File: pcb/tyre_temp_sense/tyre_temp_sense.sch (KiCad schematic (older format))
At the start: 40 parts, among them J1 Conn_01x04_Male, J2 POWER & CAN, J3 Conn_01x08_Male, J4 Conn_01x04, J5 Conn_01x04, J6 Conn_01x04, J7 Conn_01x04, J8 Conn_01x02, U1 TCA9548APWR, U2 MCP2515-xST, U3 MCP2551-I-SN, Y1 8 mhz

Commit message: Updates
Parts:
- C1, C2, C3, C4: footprint (none) -> Capacitor_SMD:C_0603_1608Metric
- J2: renamed from J3; value Conn_01x08_Male -> Extra i2c ports (no pullups); footprint (none) -> Connector_PinHeader_2.54mm:PinHeader_1x08_P2.54mm_Vertical
- J3: renamed from J1; value Conn_01x04_Male -> Analog breakout; footprint (none) -> Connector_PinHeader_2.54mm:PinHeader_1x04_P2.54mm_Vertical
- J4: value Conn_01x04 -> MUX Port 0; footprint (none) -> Connector_JST:JST_EH_B4B-EH-A_1x04_P2.50mm_Vertical
- J5: value Conn_01x04 -> MUX Port 1; footprint (none) -> Connector_JST:JST_EH_B4B-EH-A_1x04_P2.50mm_Vertical
- J6: value Conn_01x04 -> MUX Port 2; footprint (none) -> Connector_JST:JST_EH_B4B-EH-A_1x04_P2.50mm_Vertical
- J7: value Conn_01x04 -> MUX Port 3; footprint (none) -> Connector_JST:JST_EH_B4B-EH-A_1x04_P2.50mm_Vertical
- R1, R10, R11, R12, R13, R14, R2, R3, R4, R5, R6, R7, R8, R9: footprint (none) -> Resistor_SMD:R_0603_1608Metric
- TP1: renamed from TP6; value TestPoint -> CAN_H
- TP2: renamed from TP7; value TestPoint -> GND
- TP3: renamed from TP8; value TestPoint -> CAN_L
- TP4: renamed from TP9; value TestPoint -> 5V
- TP5: renamed from TP1; value TestPoint -> MOSI
- TP6: renamed from TP2; value TestPoint -> MISO
- TP7: renamed from TP3; value TestPoint -> CLK
- TP8: renamed from TP4; value TestPoint -> RX
- TP9: renamed from TP5; value TestPoint -> TX
- U2: value MCP2515-xST -> MCP2515-I/ST; LCSC (none) -> C15193
- Y1: JLCPCB Part # (none) -> C403948
- renumbered J2 to J1
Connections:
- net at U1.13 (SD4): now also J2.1 (Pin_1); no longer J2.7 (Pin_7)
- net at U1.14 (SC4): now also J2.2 (Pin_2); no longer J2.8 (Pin_8)
- net at U1.15 (SD5): now also J2.3 (Pin_3); no longer J2.5 (Pin_5)
- net at U1.16 (SC5): now also J2.4 (Pin_4); no longer J2.6 (Pin_6)
- net at U1.17 (SD6): now also J2.5 (Pin_5); no longer J2.3 (Pin_3)
- net at U1.18 (SC6): now also J2.6 (Pin_6); no longer J2.4 (Pin_4)
- net at U1.19 (SD7): now also J2.7 (Pin_7); no longer J2.1 (Pin_1)
- net at U1.20 (SC7): now also J2.8 (Pin_8); no longer J2.2 (Pin_2)
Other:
- note added: "4 pin JST connector for each temp sensor"
- note added: "AUMT tyre temperature sensing control board"
- note added: "Arduino Nano"
- note added: "CAN Controller\n"
- note added: "CAN Transceiver\n"
- note added: "Input power and CAN\n"
- moved on the sheet: A1, C1, C2, C3, C4, J1, J2, J3, J4, J5, J6, J7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

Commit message: Second revision
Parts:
- removed J2: Extra i2c ports (no pullups), Connector_PinHeader_2.54mm:PinHeader_1x08_P2.54mm_Vertical, symbol Connector:Conn_01x08_Male
- removed TP2: GND, TestPoint:TestPoint_Pad_D1.5mm, symbol Connector:TestPoint
- removed TP4: 5V, TestPoint:TestPoint_Pad_D1.5mm, symbol Connector:TestPoint
- removed TP5: MOSI, TestPoint:TestPoint_Pad_D1.5mm, symbol Connector:TestPoint
- removed TP6: MISO, TestPoint:TestPoint_Pad_D1.5mm, symbol Connector:TestPoint
- removed TP7: CLK, TestPoint:TestPoint_Pad_D1.5mm, symbol Connector:TestPoint
- added J8, J9: GND, Connector_PinHeader_2.54mm:PinHeader_1x04_P2.54mm_Vertical, symbol tyre_temp_sense-rescue:Conn_01x04_Male-Connector
- A1: symbol MCU_Module:Arduino_Nano_v3.x -> tyre_temp_sense-rescue:Arduino_Nano_v3.x-MCU_Module
- C1: renamed from C2; symbol Device:C -> tyre_temp_sense-rescue:C-Device
- C2: renamed from C3; symbol Device:C -> tyre_temp_sense-rescue:C-Device
- C3: renamed from C1; symbol Device:C -> tyre_temp_sense-rescue:C-Device
- C4: symbol Device:C -> tyre_temp_sense-rescue:C-Device
- J1: symbol Connector_Generic:Conn_01x04 -> tyre_temp_sense-rescue:Conn_01x04-Connector_Generic
- J2: renamed from J4; symbol Connector_Generic:Conn_01x04 -> tyre_temp_sense-rescue:Conn_01x04-Connector_Generic
- J3: renamed from J5; symbol Connector_Generic:Conn_01x04 -> tyre_temp_sense-rescue:Conn_01x04-Connector_Generic
- J4: renamed from J6; symbol Connector_Generic:Conn_01x04 -> tyre_temp_sense-rescue:Conn_01x04-Connector_Generic
- J5: renamed from J7; symbol Connector_Generic:Conn_01x04 -> tyre_temp_sense-rescue:Conn_01x04-Connector_Generic
- J6: renamed from J8; symbol Connector_Generic:Conn_01x02 -> tyre_temp_sense-rescue:Conn_01x02-Connector_Generic
- J7: renamed from J3; value Analog breakout -> A; symbol Connector:Conn_01x04_Male -> tyre_temp_sense-rescue:Conn_01x04_Male-Connector; Note Breakout extra analogue pins from arduino -> (none)
- R1, R10, R11, R12, R13, R2, R3, R4, R5, R6, R7, R8, R9: symbol Device:R -> tyre_temp_sense-rescue:R-Device
- R14: footprint Resistor_SMD:R_0603_1608Metric -> Resistor_SMD:R_1210_3225Metric; symbol Device:R -> tyre_temp_sense-rescue:R-Device
- TP1, TP3, TP8, TP9: symbol Connector:TestPoint -> tyre_temp_sense-rescue:TestPoint-Connector
- U1: symbol Interface_Expansion:TCA9548APWR -> tyre_temp_sense-rescue:TCA9548APWR-Interface_Expansion
- U2: symbol Interface_CAN_LIN:MCP2515-xST -> tyre_temp_sense-rescue:MCP2515-xST-Interface_CAN_LIN; LCSC C15193 -> (none)
- U3: symbol Interface_CAN_LIN:MCP2551-I-SN -> tyre_temp_sense-rescue:MCP2551-I-SN-Interface_CAN_LIN
- Y1: footprint (none) -> Crystal:Crystal_SMD_5032-2Pin_5.0x3.2mm; symbol Device:Crystal -> tyre_temp_sense-rescue:Crystal-Device; JLCPCB Part # C403948 -> C115962
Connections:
- net +3V3: now also J2.4 (Pin_4), J3.4 (Pin_4), J4.4 (Pin_4), J5.4 (Pin_4); no longer J2.2 (Pin_2), J3.2 (Pin_2), J4.2 (Pin_2), J5.2 (Pin_2)
- net +5V: now also J9.1 (Pin_1), J9.2 (Pin_2), J9.3 (Pin_3), J9.4 (Pin_4)
- net GND: now also J2.3 (Pin_3), J3.3 (Pin_3), J4.3 (Pin_3), J5.3 (Pin_3), J8.1 (Pin_1), J8.2 (Pin_2), J8.3 (Pin_3), J8.4 (Pin_4); no longer J2.1 (Pin_1), J3.1 (Pin_1), J4.1 (Pin_1), J5.1 (Pin_1)
- net A0: now reaches A1.19 (A0), J7.4 (Pin_4)
- net A1: now reaches A1.20 (A1), J7.3 (Pin_3)
- net A2: now reaches A1.21 (A2), J7.2 (Pin_2)
- net A3: now reaches A1.22 (A3), J7.1 (Pin_1)
- net at R11.2, U1.10 (SD3): now also J5.1 (Pin_1); no longer J5.4 (Pin_4)
- net at R10.2, U1.11 (SC3): now also J5.2 (Pin_2); no longer J5.3 (Pin_3)
- net at R5.2, U1.4 (SD0): now also J2.1 (Pin_1); no longer J2.4 (Pin_4)
- net at R4.2, U1.5 (SC0): now also J2.2 (Pin_2); no longer J2.3 (Pin_3)
- net at R7.2, U1.6 (SD1): now also J3.1 (Pin_1); no longer J3.4 (Pin_4)
- net at R6.2, U1.7 (SC1): now also J3.2 (Pin_2); no longer J3.3 (Pin_3)
- net at R9.2, U1.8 (SD2): now also J4.1 (Pin_1); no longer J4.4 (Pin_4)
- net at R8.2, U1.9 (SC2): now also J4.2 (Pin_2); no longer J4.3 (Pin_3)
- net CAN_H renamed CAN+
- net CAN+: now also J1.3 (Pin_3), TP3.1; no longer J1.4 (Pin_4), TP1.1
- net CAN_L renamed CAN-
- net CAN-: now also J1.4 (Pin_4), TP1.1; no longer J1.3 (Pin_3), TP3.1
- no-connect marks 20 -> 28
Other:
- note removed: "Breakout extra i2c connections\n"
- moved on the sheet: C3, J2, J3, J4, J5, J7, R1, R10, R11, R2, R3, R4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

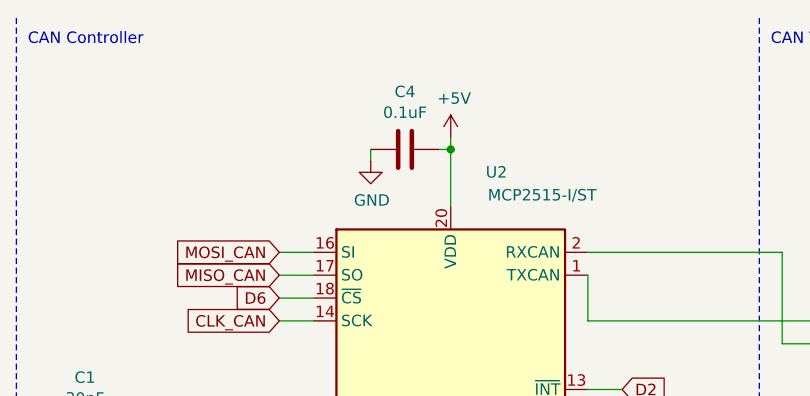
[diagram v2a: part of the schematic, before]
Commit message: Added LCSC Part info
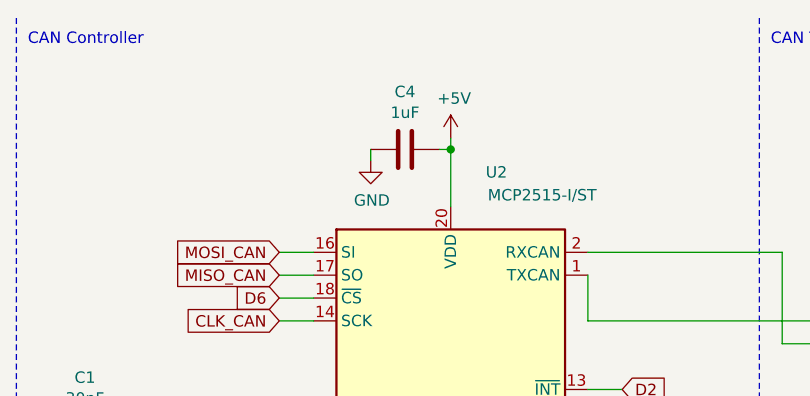
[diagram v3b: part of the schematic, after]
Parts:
- C1, C2: LCSC (none) -> C22397
- C3: LCSC (none) -> C19702
- C4: value 0.1uF -> 1uF; LCSC (none) -> C15849
- R1, R12, R13: LCSC (none) -> C25804
- R10, R11, R2, R3, R4, R5, R6, R7, R8, R9: LCSC (none) -> C23162
- R14: footprint Resistor_SMD:R_1210_3225Metric -> Resistor_SMD:R_1206_3216Metric; LCSC (none) -> C22107
- U1: LCSC (none) -> C130026
- U2: LCSC (none) -> C15193
- U3: LCSC (none) -> C49558
- Y1: JLCPCB Part # C115962 -> (none); LCSC (none) -> C115962
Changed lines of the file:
@@
 F 2 "Package_SO:TSSOP-20_4.4x6.5mm_P0.65mm" H 6650 1200 50  0001 C CIN
 F 3 "https://datasheet.lcsc.com/lcsc/1809191814_Microchip-Tech-MCP2515-I-ST_C15193.pdf" H 6750 1300 50  0001 C CNN
+F 4 "C15193" H 6650 2100 50  0001 C CNN "LCSC"
 	1    6650 2100
 	1    0    0    -1
@@
 F 1 "MCP2551-I-SN" H 8900 2500 50  0000 C CNN
 F 2 "Package_SO:SOIC-8_3.9x4.9mm_P1.27mm" H 9350 1500 50  0001 C CIN
-F 3 "http://ww1.microchip.com/downloads/en/devicedoc/21667d.pdf" H 9350 2000 50  0001 C CNN
+F 3 "https://datasheet.lcsc.com/lcsc/1809192221_Microchip-Tech-MCP2551T-I-SN_C49558.pdf" H 9350 2000 50  0001 C CNN
+F 4 "C49558" H 9350 2000 50  0001 C CNN "LCSC"
 	1    9350 2000
 	1    0    0    -1
@@
 P 6450 1050
 F 0 "C4" V 6198 1050 50  0000 C CNN
-F 1 "0.1uF" V 6289 1050 50  0000 C CNN
+F 1 "1uF" V 6289 1050 50  0000 C CNN
 F 2 "Capacitor_SMD:C_0603_1608Metric" H 6488 900 50  0001 C CNN
-F 3 "~" H 6450 1050 50  0001 C CNN
+F 3 "https://datasheet.lcsc.com/lcsc/1810261812_Samsung-Electro-Mechanics-CL10A105KB8NNNC_C15849.pdf" H 6450 1050 50  0001 C CNN
+F 4 "C15849" V 6450 1050 50  0001 C CNN "LCSC"
 	1    6450 1050
 	0    1    1    0
@@
 F 1 "30pF" V 4889 2300 50  0000 C CNN
 F 2 "Capacitor_SMD:C_0603_1608Metric" H 5088 2150 50  0001 C CNN
-F 3 "~" H 5050 2300 50  0001 C CNN
+F 3 "https://datasheet.lcsc.com/lcsc/1809300925_Samsung-Electro-Mechanics-CL10C300JB8NNNC_C22397.pdf" H 5050 2300 50  0001 C CNN
+F 4 "C22397" V 5050 2300 50  0001 C CNN "LCSC"
 	1    5050 2300
 	0    1    1    0
@@
 F 2 "Crystal:Crystal_SMD_5032-2Pin_5.0x3.2mm" H 5450 2450 50  0001 C CNN
 F 3 "https://datasheet.lcsc.com/lcsc/2103291135_Yangxing-Tech-X50328MSB2GI_C115962.pdf" H 5450 2450 50  0001 C CNN
-F 4 "C115962" V 5450 2450 50  0001 C CNN "JLCPCB Part #"
+F 4 "C115962" V 5450 2450 50  0001 C CNN "LCSC"
 	1    5450 2450
 	0    1    1    0
@@
 F 1 "30pF" V 4889 2800 50  0000 C CNN
 F 2 "Capacitor_SMD:C_0603_1608Metric" H 5088 2650 50  0001 C CNN
-F 3 "~" H 5050 2800 50  0001 C CNN
+F 3 "https://datasheet.lcsc.com/lcsc/1809300925_Samsung-Electro-Mechanics-CL10C300JB8NNNC_C22397.pdf" H 5050 2800 50  0001 C CNN
+F 4 "C22397" V 5050 2800 50  0001 C CNN "LCSC"
 	1    5050 2800
 	0    1    1    0
@@
 F 1 "10K" H 7820 2505 50  0000 L CNN
 F 2 "Resistor_SMD:R_0603_1608Metric" V 7680 2550 50  0001 C CNN
-F 3 "~" H 7750 2550 50  0001 C CNN
+F 3 "https://datasheet.lcsc.com/lcsc/1811062009_UNI-ROYAL-Uniroyal-Elec-0603WAF1002T5E_C25804.pdf" H 7750 2550 50  0001 C CNN
+F 4 "C25804" H 7750 2550 50  0001 C CNN "LCSC"
 	1    7750 2550
 	1    0    0    -1
@@
 F 1 "10K" H 8920 2405 50  0000 L CNN
 F 2 "Resistor_SMD:R_0603_1608Metric" V 8780 2450 50  0001 C CNN
-F 3 "~" H 8850 2450 50  0001 C CNN
+F 3 "https://datasheet.lcsc.com/lcsc/1811062009_UNI-ROYAL-Uniroyal-Elec-0603WAF1002T5E_C25804.pdf" H 8850 2450 50  0001 C CNN
+F 4 "C25804" H 8850 2450 50  0001 C CNN "LCSC"
 	1    8850 2450
 	1    0    0    -1
@@
 F 1 "10uF" H 5135 4245 50  0000 R CNN
 F 2 "Capacitor_SMD:C_0603_1608Metric" H 5288 4050 50  0001 C CNN
-F 3 "~" H 5250 4200 50  0001 C CNN
+F 3 "https://datasheet.lcsc.com/lcsc/1810191219_Samsung-Electro-Mechanics-CL10A106KP8NNNC_C19702.pdf" H 5250 4200 50  0001 C CNN
+F 4 "C19702" H 5250 4200 50  0001 C CNN "LCSC"
 	1    5250 4200
 	-1   0    0    1
@@
 F 1 "10K" H 4070 5055 50  0000 L CNN
 F 2 "Resistor_SMD:R_0603_1608Metric" V 3930 5100 50  0001 C CNN
-F 3 "~" H 4000 5100 50  0001 C CNN
+F 3 "https://datasheet.lcsc.com/lcsc/1811062009_UNI-ROYAL-Uniroyal-Elec-0603WAF1002T5E_C25804.pdf" H 4000 5100 50  0001 C CNN
+F 4 "C25804" H 4000 5100 50  0001 C CNN "LCSC"
 	1    4000 5100
 	1    0    0    -1
@@
 F 1 "4.7K" H 6000 4800 50  0000 L CNN
 F 2 "Resistor_SMD:R_0603_1608Metric" V 5980 4550 50  0001 C CNN
-F 3 "~" H 6050 4550 50  0001 C CNN
+F 3 "https://datasheet.lcsc.com/lcsc/1810200710_UNI-ROYAL-Uniroyal-Elec-0603WAF4701T5E_C23162.pdf" H 6050 4550 50  0001 C CNN
+F 4 "C23162" H 6050 4550 50  0001 C CNN "LCSC"
 	1    6050 4550
 	1    0    0    -1
@@
 F 1 "4.7K" H 4320 4405 50  0000 L CNN
 F 2 "Resistor_SMD:R_0603_1608Metric" V 4180 4450 50  0001 C CNN
-F 3 "~" H 4250 4450 50  0001 C CNN
+F 3 "https://datasheet.lcsc.com/lcsc/1810200710_UNI-ROYAL-Uniroyal-Elec-0603WAF4701T5E_C23162.pdf" H 4250 4450 50  0001 C CNN
+F 4 "C23162" H 4250 4450 50  0001 C CNN "LCSC"
 	1    4250 4450
 	1    0    0    -1
@@
 F 1 "4.7K" H 4620 4405 50  0000 L CNN
 F 2 "Resistor_SMD:R_0603_1608Metric" V 4480 4450 50  0001 C CNN
-F 3 "~" H 4550 4450 50  0001 C CNN
+F 3 "https://datasheet.lcsc.com/lcsc/1810200710_UNI-ROYAL-Uniroyal-Elec-0603WAF4701T5E_C23162.pdf" H 4550 4450 50  0001 C CNN
+F 4 "C23162" H 4550 4450 50  0001 C CNN "LCSC"
 	1    4550 4450
 	1    0    0    -1
@@
 F 1 "4.7K" H 6200 4800 50  0000 L CNN
 F 2 "Resistor_SMD:R_0603_1608Metric" V 6180 4550 50  0001 C CNN
-F 3 "~" H 6250 4550 50  0001 C CNN
+F 3 "https://datasheet.lcsc.com/lcsc/1810200710_UNI-ROYAL-Uniroyal-Elec-0603WAF4701T5E_C23162.pdf" H 6250 4550 50  0001 C CNN
+F 4 "C23162" H 6250 4550 50  0001 C CNN "LCSC"
 	1    6250 4550
 	1    0    0    -1
@@
 F 1 "4.7K" H 6400 4800 50  0000 L CNN
 F 2 "Resistor_SMD:R_0603_1608Metric" V 6380 4550 50  0001 C CNN
-F 3 "~" H 6450 4550 50  0001 C CNN
+F 3 "https://datasheet.lcsc.com/lcsc/1810200710_UNI-ROYAL-Uniroyal-Elec-0603WAF4701T5E_C23162.pdf" H 6450 4550 50  0001 C CNN
+F 4 "C23162" H 6450 4550 50  0001 C CNN "LCSC"
 	1    6450 4550
 	1    0    0    -1
@@
 F 1 "4.7K" H 6600 4800 50  0000 L CNN
 F 2 "Resistor_SMD:R_0603_1608Metric" V 6580 4550 50  0001 C CNN
-F 3 "~" H 6650 4550 50  0001 C CNN
+F 3 "https://datasheet.lcsc.com/lcsc/1810200710_UNI-ROYAL-Uniroyal-Elec-0603WAF4701T5E_C23162.pdf" H 6650 4550 50  0001 C CNN
+F 4 "C23162" H 6650 4550 50  0001 C CNN "LCSC"
 	1    6650 4550
 	1    0    0    -1
@@
 F 1 "4.7K" H 6800 4800 50  0000 L CNN
 F 2 "Resistor_SMD:R_0603_1608Metric" V 6780 4550 50  0001 C CNN
-F 3 "~" H 6850 4550 50  0001 C CNN
+F 3 "https://datasheet.lcsc.com/lcsc/1810200710_UNI-ROYAL-Uniroyal-Elec-0603WAF4701T5E_C23162.pdf" H 6850 4550 50  0001 C CNN
+F 4 "C23162" H 6850 4550 50  0001 C CNN "LCSC"
 	1    6850 4550
 	1    0    0    -1
@@
 F 1 "4.7K" H 7000 4800 50  0000 L CNN
 F 2 "Resistor_SMD:R_0603_1608Metric" V 6980 4550 50  0001 C CNN
-F 3 "~" H 7050 4550 50  0001 C CNN
+F 3 "https://datasheet.lcsc.com/lcsc/1810200710_UNI-ROYAL-Uniroyal-Elec-0603WAF4701T5E_C23162.pdf" H 7050 4550 50  0001 C CNN
+F 4 "C23162" H 7050 4550 50  0001 C CNN "LCSC"
 	1    7050 4550
 	1    0    0    -1
@@
 F 1 "4.7K" H 7200 4800 50  0000 L CNN
 F 2 "Resistor_SMD:R_0603_1608Metric" V 7180 4550 50  0001 C CNN
-F 3 "~" H 7250 4550 50  0001 C CNN
+F 3 "https://datasheet.lcsc.com/lcsc/1810200710_UNI-ROYAL-Uniroyal-Elec-0603WAF4701T5E_C23162.pdf" H 7250 4550 50  0001 C CNN
+F 4 "C23162" H 7250 4550 50  0001 C CNN "LCSC"
 	1    7250 4550
 	1    0    0    -1
@@
 F 1 "4.7K" H 7400 4800 50  0000 L CNN
 F 2 "Resistor_SMD:R_0603_1608Metric" V 7380 4550 50  0001 C CNN
-F 3 "~" H 7450 4550 50  0001 C CNN
+F 3 "https://datasheet.lcsc.com/lcsc/1810200710_UNI-ROYAL-Uniroyal-Elec-0603WAF4701T5E_C23162.pdf" H 7450 4550 50  0001 C CNN
+F 4 "C23162" H 7450 4550 50  0001 C CNN "LCSC"
 	1    7450 4550
 	1    0    0    -1
@@
 F 1 "TCA9548APWR" H 5650 6300 50  0000 C CNN
 F 2 "Package_SO:TSSOP-24_4.4x7.8mm_P0.65mm" H 5100 4450 50  0001 C CNN
-F 3 "http://www.ti.com/lit/ds/symlink/tca9548a.pdf" H 5150 5700 50  0001 C CNN
+F 3 "https://datasheet.lcsc.com/lcsc/1811081942_Texas-Instruments-TCA9548APWR_C130026.pdf" H 5150 5700 50  0001 C CNN
+F 4 "C130026" H 5100 5450 50  0001 C CNN "LCSC"
 	1    5100 5450
 	1    0    0    -1
@@
 F 0 "R14" H 9970 1796 50  0000 L CNN
 F 1 "120" H 9970 1705 50  0000 L CNN
-F 2 "Resistor_SMD:R_1210_3225Metric" V 9830 1750 50  0001 C CNN
-F 3 "~" H 9900 1750 50  0001 C CNN
+F 2 "Resistor_SMD:R_1206_3216Metric" V 9830 1750 50  0001 C CNN
+F 3 "https://datasheet.lcsc.com/lcsc/1810301422_UNI-ROYAL-Uniroyal-Elec-1206W4F1204T5E_C22107.pdf" H 9900 1750 50  0001 C CNN
+F 4 "C22107" H 9900 1750 50  0001 C CNN "LCSC"
 	1    9900 1750
 	1    0    0    -1
